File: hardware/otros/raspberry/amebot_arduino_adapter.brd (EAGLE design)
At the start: 43.2 x 30.5 mm, 10 parts

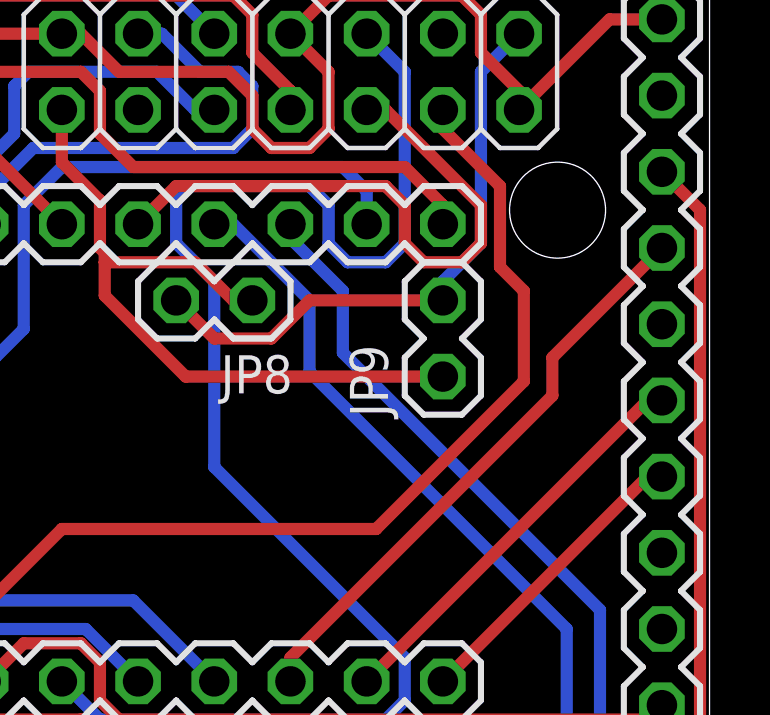
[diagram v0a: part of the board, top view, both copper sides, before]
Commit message: 
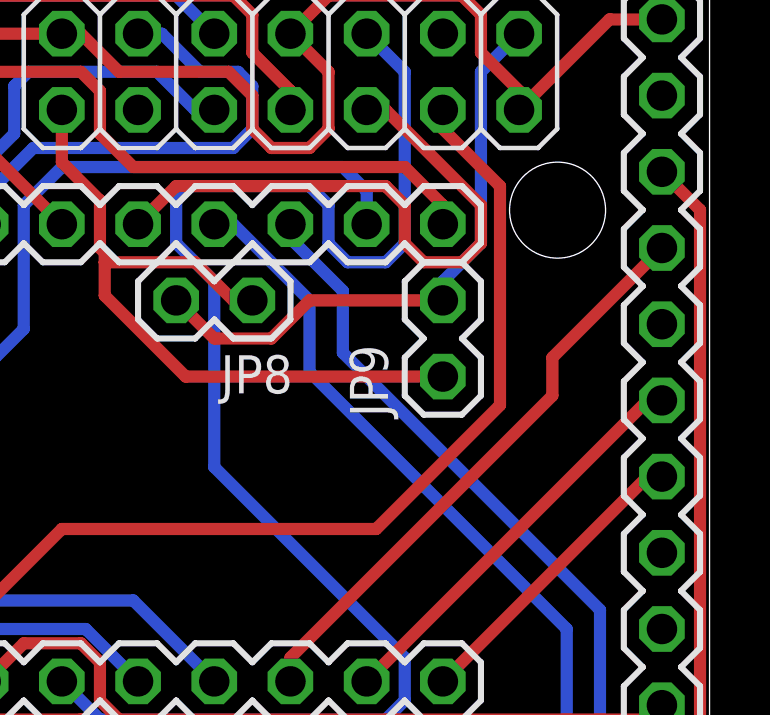
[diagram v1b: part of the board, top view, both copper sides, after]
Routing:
- net SEN5: track 34.8 -> 34.1 mm
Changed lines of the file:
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@@
 <wire x1="21.59" y1="12.22375" x2="32.0675" y2="12.22375" width="0.4064" layer="1"/>
 <wire x1="34.29" y1="25.55875" x2="34.29" y2="26.19375" width="0.4064" layer="1"/>
-<wire x1="36.98875" y1="17.145" x2="36.98875" y2="20.16125" width="0.4064" layer="1"/>
-<wire x1="36.98875" y1="20.16125" x2="36.195" y2="20.955" width="0.4064" layer="1"/>
-<wire x1="36.195" y1="20.955" x2="36.195" y2="23.65375" width="0.4064" layer="1"/>
+<wire x1="36.195" y1="16.35125" x2="36.195" y2="23.65375" width="0.4064" layer="1"/>
 <wire x1="36.195" y1="23.65375" x2="34.29" y2="25.55875" width="0.4064" layer="1"/>
-<wire x1="36.98875" y1="17.145" x2="32.0675" y2="12.22375" width="0.4064" layer="1"/>
+<wire x1="36.195" y1="16.35125" x2="32.0675" y2="12.22375" width="0.4064" layer="1"/>
 </signal>
 <signal name="SEN6">
